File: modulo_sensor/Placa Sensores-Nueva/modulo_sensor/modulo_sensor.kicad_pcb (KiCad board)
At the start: 2 copper layers, 100 x 35 mm, 33 parts, among them J1 Conn_01x08_Pin, U1 74HC14DR2G

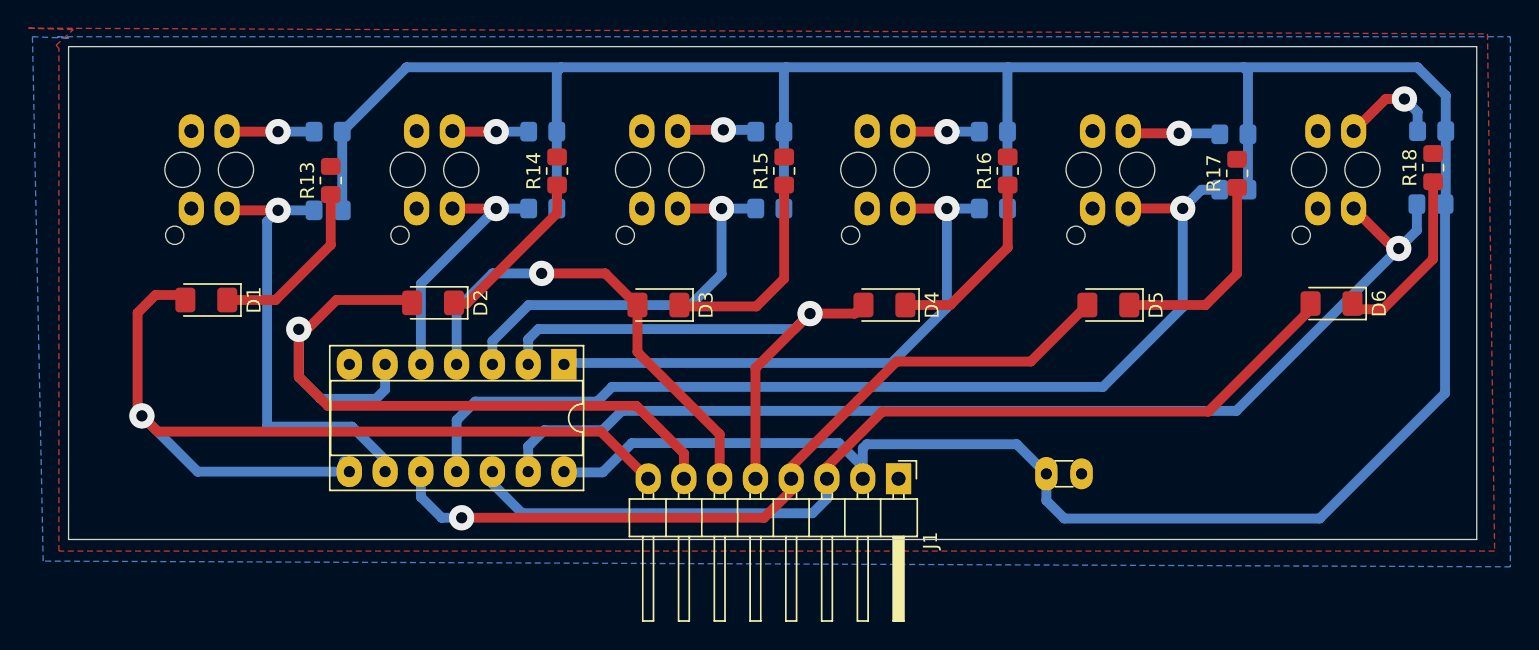
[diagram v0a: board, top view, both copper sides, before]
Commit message: Agrego pasante de GND para Schmitt Trigger
El GND del integrado queda muy aislado de todo el gnd, se agrega un pasante para soldar y asegurar que todas las tierras esten conectadas
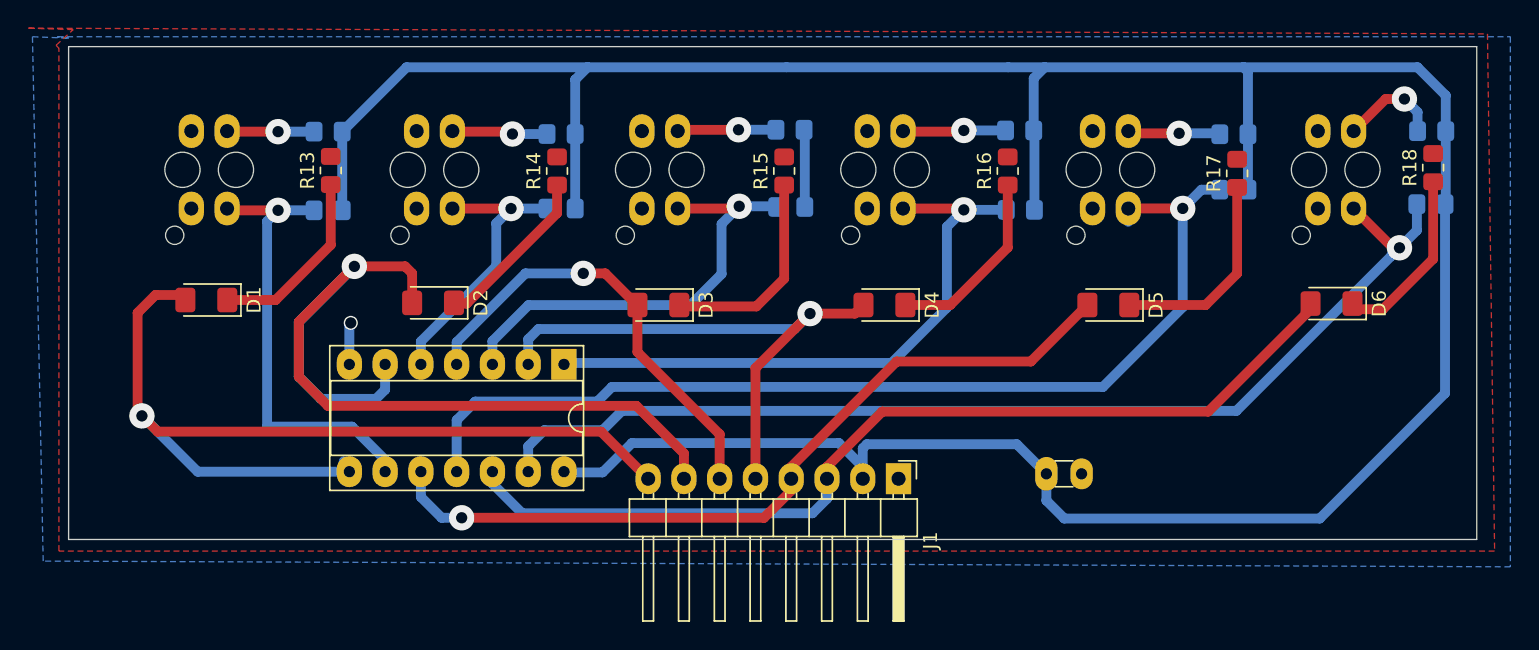
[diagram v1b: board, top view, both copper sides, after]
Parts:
- moved R8 1.92 mm to (118.2, 40.1)
- moved R7 1.86 mm to (118.1, 34.5)
- moved R6 1.49 mm to (101.9, 39.9)
- moved R5 1.44 mm to (101.8, 34.4)
- moved R3 1.31 mm to (85.5, 34.7)
- moved R4 1.30 mm to (85.5, 40.0)
- moved R13 0.71 mm to (69.2, 37.3)
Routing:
- net /Led_Sensor2: track 55.9 -> 65.4 mm
- net vcc: track 221.2 -> 217.3 mm
- net GND: track 0.00 -> 2.99 mm, vias 0 -> 1
- net /Sensor4: track 41.3 -> 43.7 mm
- net /Sensor3: track 30.1 -> 32.3 mm
- net Net-(R7-Pad1): track 5.44 -> 7.33 mm
- net /Sensor2: track 18.7 -> 20.4 mm
- net Net-(R5-Pad1): track 5.63 -> 7.01 mm
- net Net-(R3-Pad1): track 5.43 -> 6.81 mm
- net /Led_Sensor3: track 33.6 -> 32.3 mm
- net Net-(D1-K): track 12.5 -> 13.3 mm

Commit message: agrego medidas de la placa
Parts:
- moved C1 5.13 mm to (115.3, 60.9), turned to 90 degrees
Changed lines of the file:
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@@
 	(footprint "Capacitor_THT:C_Disc_D3.0mm_W1.6mm_P2.50mm"
 		(layer "F.Cu")
-		(at 120.0096 58.8772)
+		(at 115.316 60.94 90)
 		(descr "C, Disc series, Radial, pin pitch=2.50mm, , diameter*width=3.0*1.6mm^2, Capacitor, http://www.vishay.com/docs/45233/krseries.pdf")
 		(tags "C Disc series Radial pin pitch 2.50mm  diameter 3.0mm width 1.6mm Capacitor")
 		(property "Reference" "C1"
-			(at 1.5 -2 0)
+			(at 1.5 -2 90)
 			(layer "F.SilkS")
 			(hide yes)
@@
 		)
 		(property "Value" "C"
-			(at 1.25 2.05 0)
+			(at 1.25 2.05 90)
 			(layer "F.Fab")
 			(effects
@@
 		)
 		(property "Datasheet" ""
-			(at 0 0 0)
+			(at 0 0 90)
 			(unlocked yes)
 			(layer "F.Fab")
@@
 		)
 		(property "Description" "Unpolarized capacitor"
-			(at 0 0 0)
+			(at 0 0 90)
 			(unlocked yes)
 			(layer "F.Fab")
@@
 		)
 		(fp_line
-			(start -1.05 -1.05)
-			(end -1.05 1.05)
+			(start 3.55 -1.05)
+			(end -1.05 -1.05)
 			(stroke
 				(width 0.05)
@@
 		)
 		(fp_line
-			(start -1.05 1.05)
-			(end 3.55 1.05)
+			(start -1.05 -1.05)
+			(end -1.05 1.05)
 			(stroke
 				(width 0.05)
@@
 		)
 		(fp_line
-			(start 3.55 -1.05)
-			(end -1.05 -1.05)
+			(start 3.55 1.05)
+			(end 3.55 -1.05)
 			(stroke
 				(width 0.05)
@@
 		)
 		(fp_line
-			(start 3.55 1.05)
-			(end 3.55 -1.05)
+			(start -1.05 1.05)
+			(end 3.55 1.05)
 			(stroke
 				(width 0.05)
@@
 		)
 		(fp_line
-			(start -0.25 -0.8)
-			(end -0.25 0.8)
+			(start 2.75 -0.8)
+			(end -0.25 -0.8)
 			(stroke
 				(width 0.1)
@@
 		)
 		(fp_line
-			(start -0.25 0.8)
-			(end 2.75 0.8)
+			(start -0.25 -0.8)
+			(end -0.25 0.8)
 			(stroke
 				(width 0.1)
@@
 		)
 		(fp_line
-			(start 2.75 -0.8)
-			(end -0.25 -0.8)
+			(start 2.75 0.8)
+			(end 2.75 -0.8)
 			(stroke
 				(width 0.1)
@@
 		)
 		(fp_line
-			(start 2.75 0.8)
-			(end 2.75 -0.8)
+			(start -0.25 0.8)
+			(end 2.75 0.8)
 			(stroke
 				(width 0.1)
@@
 		)
 		(fp_text user "${REFERENCE}"
-			(at 1.25 0 0)
+			(at 1.25 0 90)
 			(layer "F.Fab")
 			(effects
@@
 		)
 		(pad "1" thru_hole oval
-			(at 0 0)
+			(at 0 0 90)
 			(size 1.6 2.4)
 			(drill 0.8)
@@
 		)
 		(pad "2" thru_hole oval
-			(at 2.5 0)
+			(at 2.5 0 90)
 			(size 1.6 2.2)
 			(drill 0.8)
@@
 		)
 		(fill no)
+		(locked yes)
 		(layer "Edge.Cuts")
 	)
@@
 		(layer "Edge.Cuts")
 		(pts
-			(xy 50.5712 66.04) (xy 83.0712 66.04)
+			(xy 150.5712 28.54) (xy 150.5712 63.54)
+		)
+		(height 12.1412)
+		(orientation 1)
+		(format
+			(prefix "")
+			(suffix "")
+			(units 3)
+			(units_format 1)
+			(precision 4)
+		)
+		(style
+			(thickness 0.05)
+			(arrow_length 1.27)
+			(text_position_mode 0)
+			(arrow_direction outward)
+			(extension_height 0.58642)
+			(extension_offset 0.5)
+			(keep_text_aligned yes)
+		)
+		(gr_text "35,0000 mm"
+			(at 161.5624 46.04 90)
+			(layer "Edge.Cuts")
+			(effects
+				(font
+					(size 1 1)
+					(thickness 0.15)
+				)
+			)
 		)
-		(height 24.6888)
+	)
+	(dimension
+		(type orthogonal)
+		(layer "Edge.Cuts")
+		(pts
+			(xy 50.5712 63.54) (xy 150.5712 63.54)
+		)
+		(height 24.4456)
 		(orientation 0)
 		(format
@@
 			(keep_text_aligned yes)
 		)
-		(gr_text "32,5000 mm"
-			(at 66.8212 89.5788 0)
+		(gr_text "100,0000 mm"
+			(at 100.5712 86.8356 0)
 			(layer "Edge.Cuts")
 			(effects
@@
 	)
 	(segment
-		(start 117.2972 30.007)
+		(start 103.6828 30.007)
 		(end 101.5492 30.007)
 		(width 0.7)
@@
 	)
 	(segment
+		(start 102.8032 30.8866)
+		(end 103.6828 30.007)
+		(width 0.7)
+		(layer "B.Cu")
+		(net 1)
+	)
+	(segment
+		(start 115.316 60.94)
+		(end 139.3644 60.94)
+		(width 0.7)
+		(layer "B.Cu")
+		(net 1)
+	)
+	(segment
 		(start 86.5472 34.7472)
 		(end 86.5472 30.8866)
@@
 	)
 	(segment
-		(start 148.3708 32.009776)
-		(end 146.368024 30.007)
+		(start 139.3644 60.94)
+		(end 148.32 51.9844)
 		(width 0.7)
 		(layer "B.Cu")
@@
 	)
 	(segment
-		(start 134.3246 34.7632)
-		(end 134.3246 30.3212)
+		(start 117.2972 30.007)
+		(end 103.6828 30.007)
 		(width 0.7)
 		(layer "B.Cu")
@@
 	)
 	(segment
-		(start 106.9698 57.0646)
-		(end 107.2588 56.7756)
+		(start 148.3708 32.009776)
+		(end 146.368024 30.007)
 		(width 0.7)
 		(layer "B.Cu")
@@
 	)
 	(segment
-		(start 148.32 53.1528)
-		(end 148.32 39.7256)
+		(start 134.3246 34.7632)
+		(end 134.3246 30.3212)
+		(width 0.7)
+		(layer "B.Cu")
+		(net 1)
+	)
+	(segment
+		(start 106.9698 60.9886)
+		(end 107.4588 61.4776)
 		(width 0.7)
 		(layer "B.Cu")
@@
 	)
 	(segment
-		(start 121.2838 62.0514)
-		(end 139.4214 62.0514)
+		(start 90.5764 56.6928)
+		(end 105.279395 56.6928)
 		(width 0.7)
 		(layer "B.Cu")
@@
 	)
 	(segment
-		(start 90.5764 56.6928)
-		(end 105.279395 56.6928)
+		(start 70.003617 34.5772)
+		(end 74.573817 30.007)
 		(width 0.7)
 		(layer "B.Cu")
@@
 	)
 	(segment
-		(start 70.003617 34.5772)
-		(end 74.573817 30.007)
+		(start 148.32 51.9844)
+		(end 148.32 39.7256)
 		(width 0.7)
 		(layer "B.Cu")
@@
 	)
 	(segment
-		(start 117.908 56.7756)
-		(end 120.0096 58.8772)
+		(start 114.7784 61.4776)
+		(end 115.316 60.94)
 		(width 0.7)
 		(layer "B.Cu")
@@
 	)
 	(segment
-		(start 107.2588 56.7756)
-		(end 117.908 56.7756)
-		(width 0.7)
-		(layer "B.Cu")
-		(net 1)
-	)
-	(segment
 		(start 88.4936 58.7756)
 		(end 90.5764 56.6928)
@@
 	)
 	(segment
-		(start 139.4214 62.0514)
-		(end 148.32 53.1528)
-		(width 0.7)
-		(layer "B.Cu")
-		(net 1)
-	)
-	(segment
 		(start 119.888 30.007)
 		(end 117.2972 30.007)
@@
 	)
 	(segment
+		(start 102.8032 34.4424)
+		(end 102.8032 30.8866)
+		(width 0.7)
+		(layer "B.Cu")
+		(net 1)
+	)
+	(segment
 		(start 134.3246 34.7632)
 		(end 134.3246 38.7002)
@@
 	)
 	(segment
-		(start 70.003617 34.5772)
-		(end 70.003617 40.1652)
-		(width 0.7)
-		(layer "B.Cu")
-		(net 1)
-	)
-	(segment
-		(start 120.0096 60.7772)
-		(end 121.2838 62.0514)
+		(start 106.9698 59.2266)
+		(end 106.9698 60.9886)
 		(width 0.7)
 		(layer "B.Cu")
@@
 	)
 	(segment
-		(start 120.0096 58.8772)
-		(end 120.0096 60.7772)
+		(start 70.003617 34.5772)
+		(end 70.003617 40.1652)
 		(width 0.7)
 		(layer "B.Cu")
@@
 	)
 	(segment
-		(start 106.9698 59.2266)
-		(end 106.9698 57.0646)
+		(start 107.4588 61.4776)
+		(end 114.7784 61.4776)
 		(width 0.7)
 		(layer "B.Cu")

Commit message: Update modulo_sensor.kicad_pcb
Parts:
- moved R10 1.23 mm to (133.3, 39.9)
- moved R9 0.27 mm to (133.3, 34.5)
- moved R3 0.25 mm to (85.5, 34.5)
- moved R18 0.24 mm to (147.5, 37.4)
- moved R2 0.24 mm to (69.0, 39.9)
- moved R12 0.20 mm to (147.3, 39.9)
- moved D1 0.20 mm to (60.4, 46.7)
- moved R8 0.20 mm to (118.2, 39.9)
- moved R17 0.17 mm to (133.6, 37.4)
- moved D3 0.16 mm to (92.4, 46.7)
- moved D4 0.15 mm to (108.5, 46.7)
- moved D5 0.15 mm to (124.4, 46.7)
- moved R4 0.11 mm to (85.5, 39.9)
- moved R1 0.08 mm to (69.0, 34.5)
- moved D6 0.05 mm to (140.3, 46.7)
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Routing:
- net /Led_Sensor1: track 65.8 -> 54.3 mm
- net /Sensor6: track 77.6 -> 80.5 mm
- net /Sensor1: track 32.1 -> 30.5 mm
- net /Led_Sensor2: track 65.4 -> 64.4 mm
- net /Sensor5: track 73.5 -> 73.0 mm

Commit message: detalles
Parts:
- moved C1 0.98 mm to (114.5, 61.4)
- moved D2 0.51 mm to (76.4, 46.2)
- moved D1 0.51 mm to (60.4, 46.2)
- moved D3 0.51 mm to (92.4, 46.2)
- moved D4 0.51 mm to (108.5, 46.2)
- moved D5 0.51 mm to (124.4, 46.2)
- moved D6 0.51 mm to (140.3, 46.2)
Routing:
- net /Led_Sensor2: track 64.4 -> 53.7 mm
- net /Led_Sensor5: track 57.0 -> 59.5 mm
- net /Led_Sensor6: track 67.5 -> 69.9 mm
- net /Led_Sensor3: track 32.1 -> 34.2 mm
- net /Led_Sensor4: track 40.0 -> 39.4 mm
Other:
- board text added: "CDR FIUBA"
